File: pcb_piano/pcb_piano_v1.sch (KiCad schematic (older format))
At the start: 21 parts

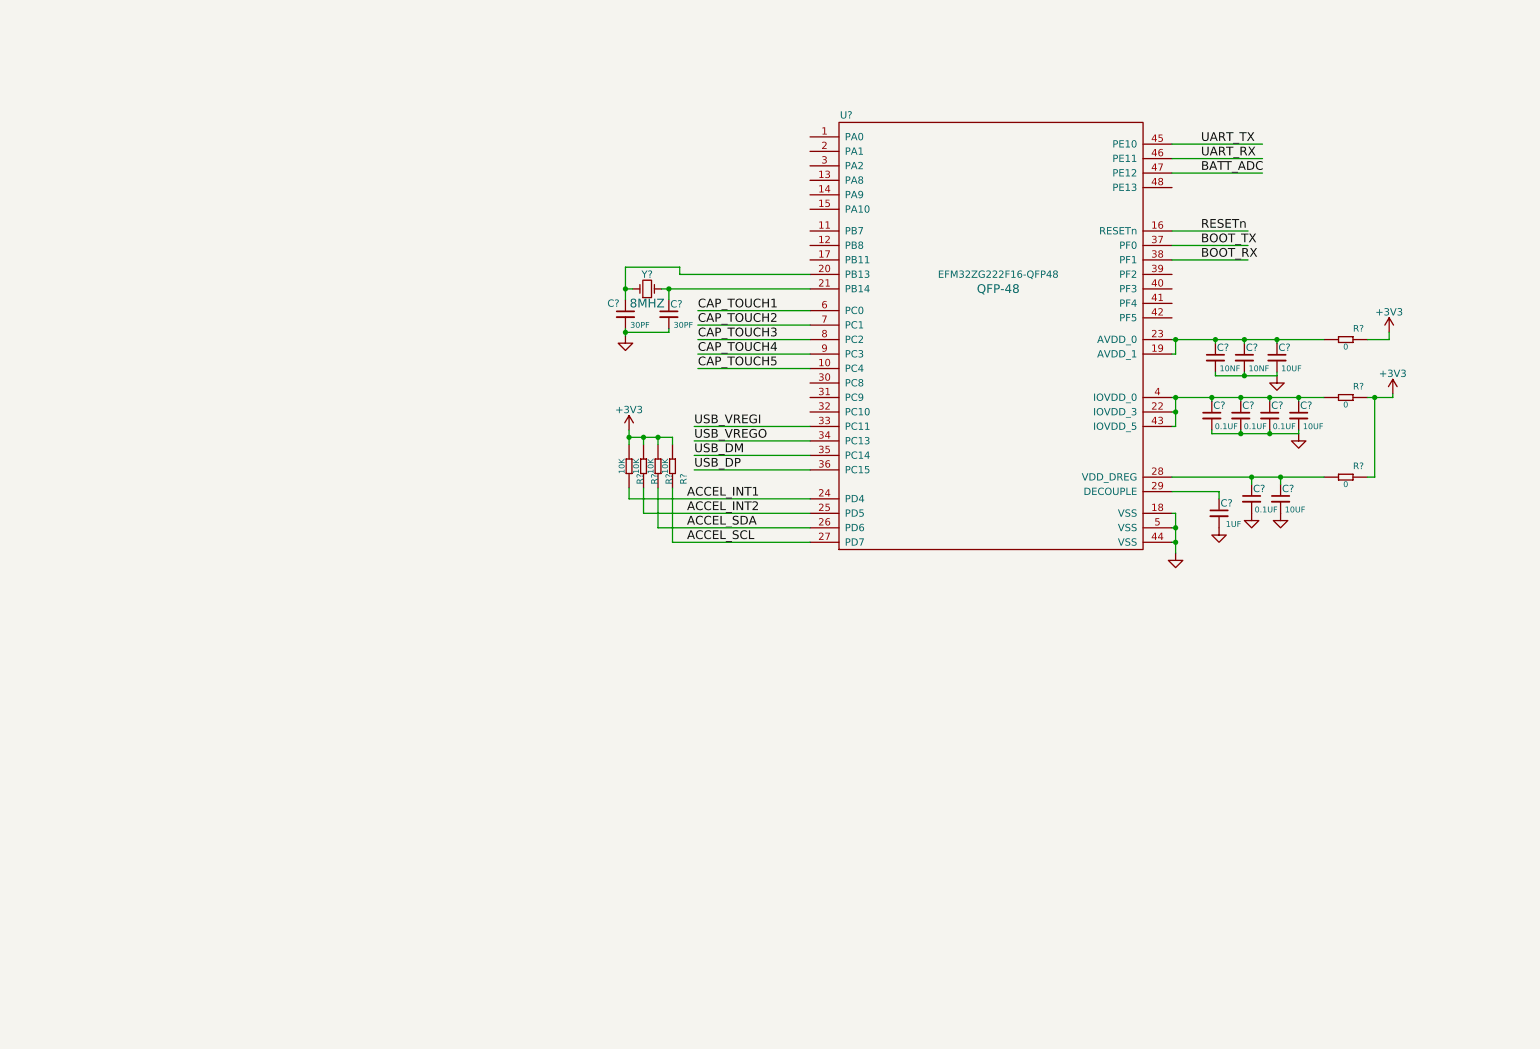
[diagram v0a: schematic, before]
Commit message: Progress on schematic. Added happy gecko, regulator, and cap touch
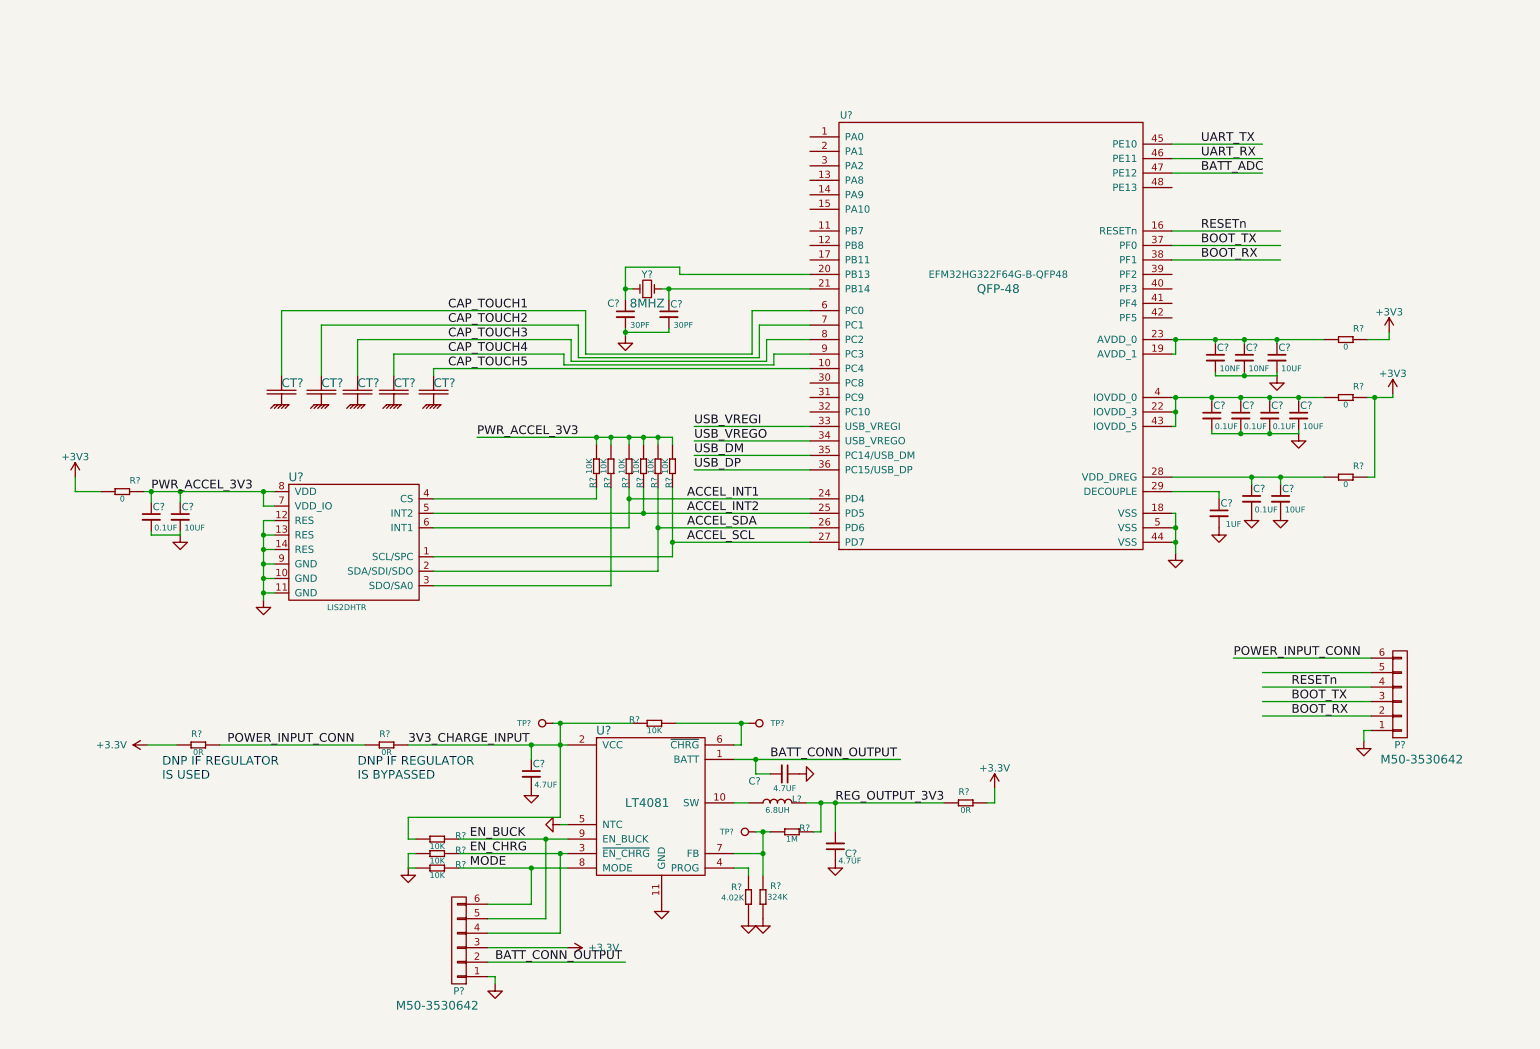
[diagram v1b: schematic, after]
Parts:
- removed U?: connex_EFM32ZG222F16-QFP48, Housings_QFP:TQFP-48_7x7mm_Pitch0.5mm, symbol connex_EFM32ZG222F16-QFP48
- added C?: CONNEX-SMD-CAP-10UF-0402, Capacitors_SMD:C_0402, symbol CONNEX-SMD-CAP-10UF-0402
- added C?: CONNEX-SMD-CAP-100NF-0402, Capacitors_SMD:C_0402, symbol CONNEX-SMD-CAP-100NF-0402
- added C? (x3): CONNEX-SMD-CAP-4700NF-0603, Capacitors_SMD:C_0603, symbol CONNEX-SMD-CAP-4700NF-0603
- added CT? (x5): CONNEX-CAPTOUCH-BUTTON-SINGLE, symbol CONNEX-CAPTOUCH-BUTTON-SINGLE
- added L?: CONNEX-SMD-INDUCTOR-6R8M-0603, connex_inductor:L_0603, symbol CONNEX-SMD-INDUCTOR-6R8M-0603
- added P? (x2): CONN_01X06_M50-3530642, Pin_Headers:Pin_Header_Straight_1x06, symbol CONN_01X06_M50-3530642
- added R? (x2): CONNEX-SMD-RES-10K-0603, R0603, symbol CONNEX-SMD-RES-10K-0603
- added R?: CONNEX-SMD-RES-0-0603, R0603, symbol CONNEX-SMD-RES-0-0603
- added R? (x3): SMD-RES-0R-1_4W_0603_, Resistors_SMD:R_0603, symbol SMD-RES-0R-1_4W_0603_
- added R? (x4): SMD-RES-10K-1%-1_10W_0603_, Resistors_SMD:R_0603, symbol SMD-RES-10K-1%-1_10W_0603_
- added R?: CONNEX-SMD-RES-324K-0603, Resistors_SMD:R_0603, symbol CONNEX-SMD-RES-324K-0603
- added R?: CONNEX-SMD-RES-1M-0603, Resistors_SMD:R_0603, symbol CONNEX-SMD-RES-1M-0603
- added R?: CONNEX-SMD-RES-4K02-0603, Resistors_SMD:R_0603, symbol CONNEX-SMD-RES-4K02-0603
- added TP? (x3): test_point_smt, connex_test:TEST_POINT_SMD_50MIL, symbol test_point_smt
- added U?: connex-accel-LIS2DHTR, symbol connex-accel-LIS2DHTR
- added U?: CONNEX_REGUL_LT4081, connex_smd_misc:CONNEX_DFN_10PIN_3MMX3MM, symbol CONNEX_REGUL_LT4081
- added U?: connex_EFM32HG322F64G-B-QFP48, Housings_QFP:TQFP-48_7x7mm_Pitch0.5mm, symbol connex_EFM32HG322F64G-B-QFP48
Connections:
- net labels added: +3.3V, 3V3_CHARGE_INPUT, BATT_CONN_OUTPUT, EN_BUCK, EN_CHRG, MODE, POWER_INPUT_CONN, PWR_ACCEL_3V3, REG_OUTPUT_3V3
- wire segments 77 -> 175
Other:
- note added: "DNP IF REGULATOR \nIS BYPASSED"
- note added: "DNP IF REGULATOR \nIS USED"

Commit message: Added usb charging, ferrite bead, and piezo, began layout
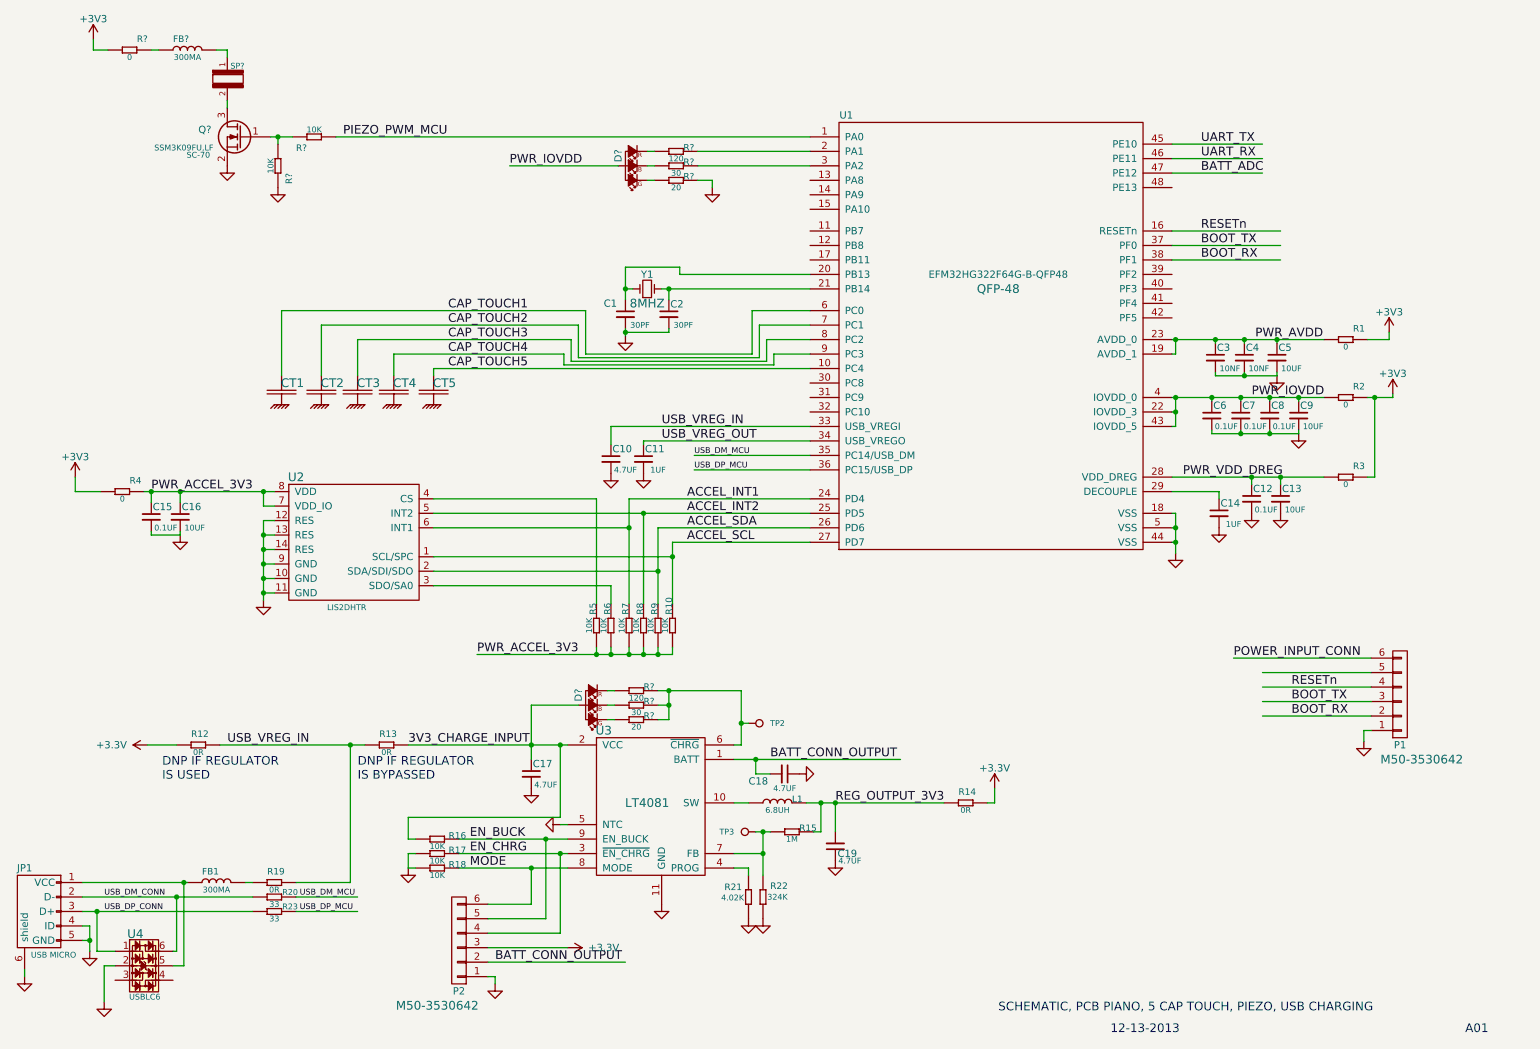
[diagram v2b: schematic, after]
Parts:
- removed C? (x2): CONNEX-SMD-CAP-30PF-0603, 0603, symbol CONNEX-SMD-CAP-30PF-0603
- removed R?: SMD-RES-10K-1%-1_10W_0603_, Resistors_SMD:R_0603, symbol SMD-RES-10K-1%-1_10W_0603_
- removed TP?: test_point_smt, connex_test:TEST_POINT_SMD_50MIL, symbol test_point_smt
- added C1, C2: CONNEX-SMD-CAP-30PF-0402, Capacitors_SMD:C_0402, symbol CONNEX-SMD-CAP-30PF-0402
- added C10: CONNEX-SMD-CAP-4700NF-0603, Capacitors_SMD:C_0603, symbol CONNEX-SMD-CAP-4700NF-0603
- added C11: CONNEX-SMD-CAP-1UF-0402, Capacitors_SMD:C_0402, symbol CONNEX-SMD-CAP-1UF-0402
- added D? (x2): LED_RGB_SMLP34RGB1W3, symbol LED_RGB_SMLP34RGB1W3
- added FB1, FB?: CONNEX-SMD-FERRITE-BEAD-300MA-BLM15AG102SN1D, connex_inductor:L_0402, symbol CONNEX-SMD-FERRITE-BEAD-300MA-BLM15AG102SN1D
- added JP1: connex_usb_micro_b_10103594-0001LF, Connect:USB_Micro-B_10103594-0001LF, symbol connex_usb_micro_b_10103594-0001LF
- added Q?: Q_NMOS_SSM3K09FULF, symbol Q_NMOS_SSM3K09FULF
- added R19: SMD-RES-0R-1_4W_0603_, Resistors_SMD:R_0603, symbol SMD-RES-0R-1_4W_0603_
- added R20, R23: CONNEX-SMD-RES-33-0402, Resistors_SMD:R_0402, symbol CONNEX-SMD-RES-33-0402
- added R? (x2): CONNEX-SMD-RES-10K-0603, Resistors_SMD:R_0603, symbol CONNEX-SMD-RES-10K-0603
- added R?: CONNEX-SMD-RES-0-0603, Resistors_SMD:R_0603, symbol CONNEX-SMD-RES-0-0603
- added R? (x2): CONNEX-SMD-RES-20-0603, R0603, symbol CONNEX-SMD-RES-20-0603
- added R? (x2): CONNEX-SMD-RES-30-0603, R0603, symbol CONNEX-SMD-RES-30-0603
- added R? (x2): CONNEX-SMD-RES-120-0603, R0603, symbol CONNEX-SMD-RES-120-0603
- added SP?: connex-piezo-4khz-AT-2440-TWT-R, symbol connex-piezo-4khz-AT-2440-TWT-R
- added U4: CONNEX-DIODE-TVS-USB-USBLC6-4SC6Y, TO_SOT_Packages_SMD:SOT-23-6, symbol CONNEX-DIODE-TVS-USB-USBLC6-4SC6Y
- C14, C3, C4: renamed from C?; footprint 0402 -> Capacitors_SMD:C_0402
- CT1, CT2, CT3, CT4, CT5: renamed from CT?; footprint (none) -> connex_cap_touch:CONNEX-CAPTOUCH-SINGLE-BUTTON-20MM
- R1, R10, R2, R3, R4, R5, R6, R7, R8, R9: renamed from R?; footprint R0603 -> Resistors_SMD:R_0603
- U2: renamed from U?; footprint (none) -> connex_smd_misc:CONNEX_DFN_10PIN_3MMX3MM
- Y1: renamed from Y?; footprint (none) -> connex_crystal:CONNEX_CRYSTAL_4SMD_32X50
- gave numbers to parts that had none: 28
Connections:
- net labels added: PIEZO_PWM_MCU, PWR_AVDD, PWR_IOVDD, PWR_VDD_DREG, USB_DM_CONN, USB_DM_MCU, USB_DP_CONN, USB_DP_MCU, USB_VREG_IN, USB_VREG_OUT
- net labels removed: USB_DM, USB_DP, USB_VREGI, USB_VREGO
- wire segments 175 -> 222
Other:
- note added: "12-13-2013"
- note added: "A01"
- note added: "SCHEMATIC, PCB PIANO, 5 CAP TOUCH, PIEZO, USB CHARGING"
- moved on the sheet: R10, R5, R6, R7, R8, R9

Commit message: Pushed Version 1 hardware
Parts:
- removed P2: CONN_01X06_M50-3530642, Pin_Headers:Pin_Header_Straight_1x06, symbol CONN_01X06_M50-3530642
- removed R12: SMD-RES-0R-1_4W_0603_, Resistors_SMD:R_0603, symbol SMD-RES-0R-1_4W_0603_
- removed R22: CONNEX-SMD-RES-324K-0603, Resistors_SMD:R_0603, symbol CONNEX-SMD-RES-324K-0603
- removed R?: CONNEX-SMD-RES-10K-0603, Resistors_SMD:R_0603, symbol CONNEX-SMD-RES-10K-0603
- added J1: CONNEX_CONN_2PIN_KEYED, connex_connectors:CONNEX_CONN-2POS-KEYED-S2B-PH-K-S, symbol CONNEX_CONN_2PIN_KEYED
- added R12: CONNEX-SMD-RES-1M-0603, Resistors_SMD:R_0603, symbol CONNEX-SMD-RES-1M-0603
- added R22, R32: CONNEX-SMD-RES-324K-0402, Resistors_SMD:R_0402, symbol CONNEX-SMD-RES-324K-0402
- added R26: SMD-RES-10K-1%-1_10W_0603_, Resistors_SMD:R_0603, symbol SMD-RES-10K-1%-1_10W_0603_
- added R33: CONNEX-SMD-RES-634k-0402, Resistors_SMD:R_0402, symbol CONNEX-SMD-RES-634k-0402
- added R34, R35: CONNEX-SMD-RES-10K-0603, Resistors_SMD:R_0603, symbol CONNEX-SMD-RES-10K-0603
- added TP1, TP10, TP11, TP4, TP5, TP6, TP7, TP8, TP9: test_point_smt, connex_diodes:TEST_POINT_SMD_50MIL, symbol test_point_smt
- CT1, CT2, CT3, CT4, CT5: footprint connex_cap_touch:CONNEX-CAPTOUCH-SINGLE-BUTTON-20MM -> connex_cap_touch:CONNEX-CAPTOUCH-SINGLE-BUTTON-15MM
- D1, D2: renamed from D?; footprint (none) -> connex_led:led_0404_SMLP34RGB1W3
- Q1: renamed from Q?; footprint (none) -> TO_SOT_Packages_SMD:SC-70
- R25, R27, R28, R29, R30, R31: renamed from R?; footprint R0603 -> Resistors_SMD:R_0603
- SP1: renamed from SP?; footprint (none) -> connex_device:CONNEX-PIEZO-AT-2440-TWT-R
- TP2, TP3: footprint connex_test:TEST_POINT_SMD_50MIL -> connex_diodes:TEST_POINT_SMD_50MIL
- U2: footprint connex_smd_misc:CONNEX_DFN_10PIN_3MMX3MM -> connex_smd_misc:CONNEX_LGA-14_2MMX2MM
- gave numbers to parts that had none: 3
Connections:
- net labels added: EN_BUCK_MCU, STAT_LED_B, STAT_LED_R, USB_VBUS_CONN, USB_VBUS_IN
- net labels removed: 3V3_CHARGE_INPUT, POWER_INPUT_CONN
- wire segments 222 -> 232
- no-connect marks 0 -> 13
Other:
- note added: "TODO: CHANGE RESISTORS VALUES ON LED"
- note removed: "DNP IF REGULATOR \nIS BYPASSED"
- note removed: "DNP IF REGULATOR \nIS USED"
- moved on the sheet: D1, R13, R16, R25, R27, R28, TP2
